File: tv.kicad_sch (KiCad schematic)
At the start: 38 parts, among them IC1 CXA1145, IC29 74HC4024, IC30 74HC10, U1 Conn_01x07, X1 4.433619MHz

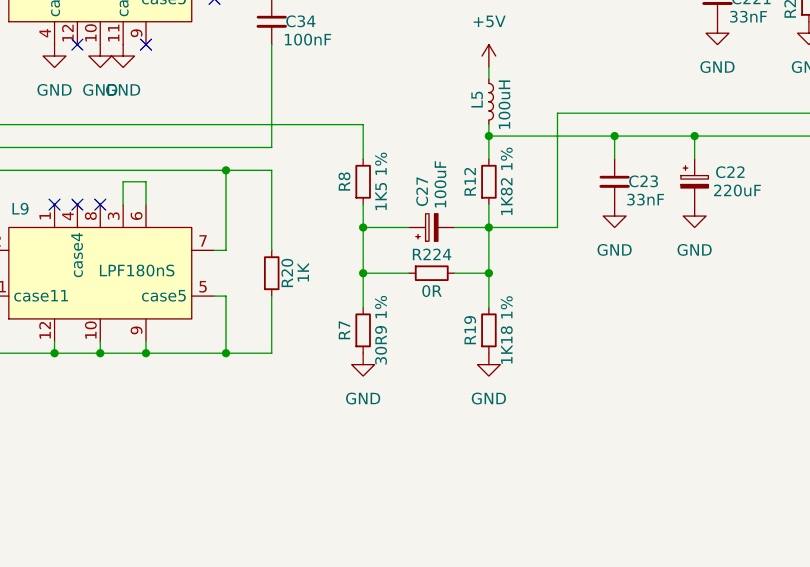
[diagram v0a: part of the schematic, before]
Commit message: video and keyboard routing
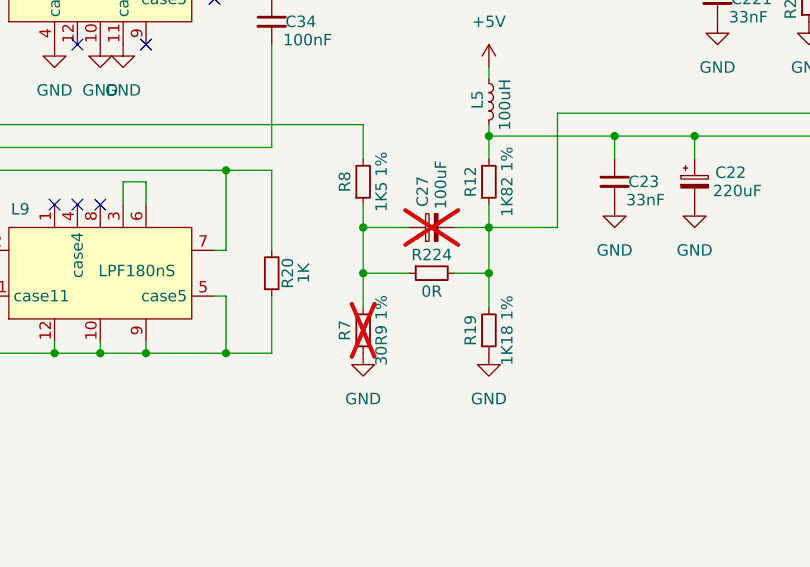
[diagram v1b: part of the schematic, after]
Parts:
- C25: footprint (none) -> Acorn:Trim_Capacitor
- C27: footprint Capacitor_THT:CP_Radial_D5.0mm_P2.50mm -> Capacitor_THT:CP_Radial_Tantal_D6.0mm_P5.00mm; now not fitted
- R7: now not fitted
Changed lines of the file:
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@@
 		(in_bom yes)
 		(on_board yes)
-		(dnp no)
+		(dnp yes)
 		(property "Reference" "R7"
 			(at 182.118 86.36 90)
@@
 		(in_bom yes)
 		(on_board yes)
-		(dnp no)
+		(dnp yes)
 		(property "Reference" "C27"
 			(at 190.754 72.644 0)
@@
 			)
 		)
-		(property "Footprint" "Capacitor_THT:CP_Radial_D5.0mm_P2.50mm"
+		(property "Footprint" "Capacitor_THT:CP_Radial_Tantal_D6.0mm_P5.00mm"
 			(at 191.77 74.93 0)
 			(effects
@@
 			)
 		)
-		(property "Footprint" ""
+		(property "Footprint" "Acorn:Trim_Capacitor"
 			(at 69.85 58.42 0)
 			(effects

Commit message: yet more traces
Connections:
- net TV_Sound: now also C220.2; no longer C220.1
- net at C221.1, R210.1, R211.2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: now also C220.1; no longer C220.2
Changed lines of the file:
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@@
 		(lib_id "Device:C_Polarized_Small")
 		(at 218.44 38.1 0)
+		(mirror x)
 		(unit 1)
 		(exclude_from_sim no)
@@
 		(dnp no)
 		(property "Reference" "C220"
-			(at 220.726 37.084 0)
+			(at 220.726 39.116 0)
 			(effects
 				(font
@@
 		)
 		(property "Value" "10uF"
-			(at 220.472 39.116 0)
+			(at 220.472 37.084 0)
 			(effects
 				(font

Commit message: keyboard routing
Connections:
- net +5V: now also IC30.14 (VCC)
- net GND: now also IC30.10, IC30.11, IC30.7 (GND), IC30.9
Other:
- moved on the sheet: IC30D

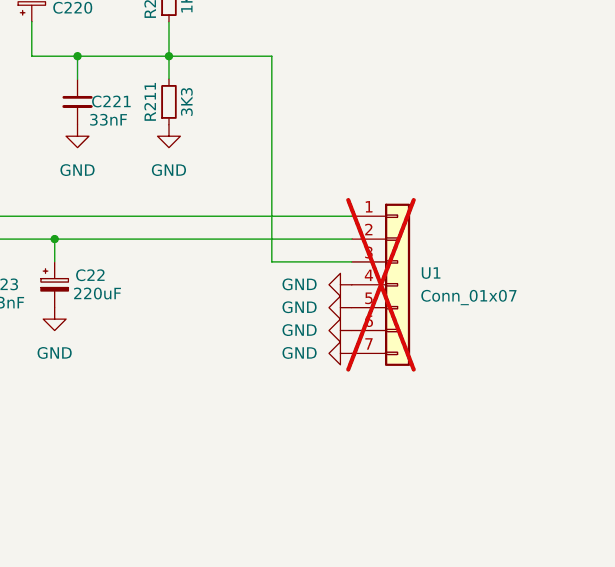
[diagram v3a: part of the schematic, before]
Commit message: progress power and keyboard
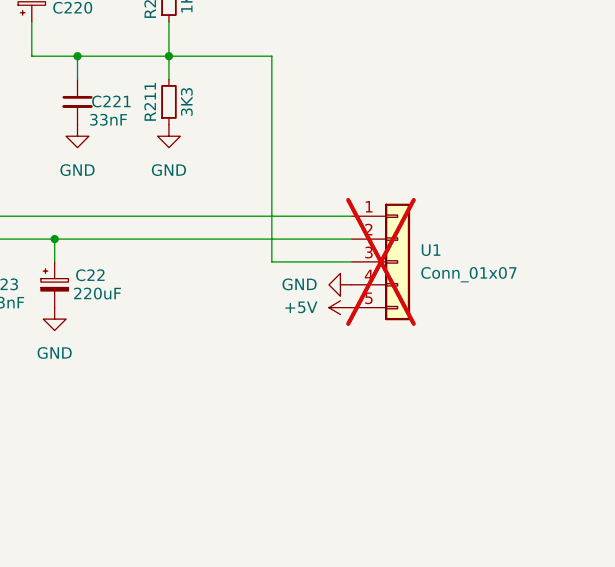
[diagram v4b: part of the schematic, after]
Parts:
- R12, R19, R7, R8: footprint Resistor_SMD:R_0805_2012Metric -> Resistor_SMD:R_1206_3216Metric
- U1: footprint Connector_PinSocket_2.54mm:PinSocket_1x07_P2.54mm_Vertical -> Connector_PinSocket_2.54mm:PinSocket_1x05_P2.54mm_Vertical; symbol Connector_Generic:Conn_01x07 -> Connector_Generic:Conn_01x05
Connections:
- net +5V: now also U1.5 (Pin_5)
- net GND: no longer U1.5 (Pin_5), U1.6 (Pin_6), U1.7 (Pin_7)

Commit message: analogue video
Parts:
- added R14: 1K, Resistor_SMD:R_0805_2012Metric, symbol Device:R_Small
- C33: footprint Capacitor_THT:CP_Radial_D5.0mm_P2.50mm -> Capacitor_THT:CP_Radial_Tantal_D4.5mm_P5.00mm
- IC1: footprint Package_SO:SOIC-24W_7.5x15.4mm_P1.27mm -> Package_SO:SOJ-24_7.62x15.875mm_P1.27mm
- L9: footprint (none) -> Acorn:LPF180nS
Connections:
- net GND: now also C25.1, R14.1; no longer C25.2
- net at C34.1, L7.7: now also R14.2
- net at IC1.6 (XIN), X1.1: now also C25.2; no longer C25.1
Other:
- moved on the sheet: C34
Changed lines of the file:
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@@
 	)
 	(junction
+		(at 171.45 44.45)
+		(diameter 0)
+		(color 0 0 0 0)
+	)
+	(junction
 		(at 120.65 88.9)
 		(diameter 0)
@@
 	(wire
 		(pts
+			(xy 171.45 44.45) (xy 180.34 44.45)
+		)
+		(stroke
+			(width 0)
+			(type default)
+		)
+	)
+	(wire
+		(pts
 			(xy 160.02 88.9) (xy 160.02 87.63)
 		)
@@
 	(wire
 		(pts
-			(xy 173.99 54.61) (xy 173.99 66.04)
+			(xy 171.45 54.61) (xy 171.45 66.04)
 		)
 		(stroke
@@
 	(wire
 		(pts
+			(xy 180.34 54.61) (xy 180.34 57.15)
+		)
+		(stroke
+			(width 0)
+			(type default)
+		)
+	)
+	(wire
+		(pts
 			(xy 194.31 74.93) (xy 198.12 74.93)
 		)
@@
 	(wire
 		(pts
-			(xy 173.99 44.45) (xy 167.64 44.45)
+			(xy 171.45 44.45) (xy 167.64 44.45)
 		)
 		(stroke
@@
 	(wire
 		(pts
-			(xy 173.99 49.53) (xy 173.99 44.45)
+			(xy 171.45 49.53) (xy 171.45 44.45)
 		)
 		(stroke
@@
 	(wire
 		(pts
-			(xy 134.62 66.04) (xy 173.99 66.04)
+			(xy 134.62 66.04) (xy 171.45 66.04)
 		)
 		(stroke
@@
 	(wire
 		(pts
+			(xy 180.34 44.45) (xy 180.34 49.53)
+		)
+		(stroke
+			(width 0)
+			(type default)
+		)
+	)
+	(wire
+		(pts
 			(xy 132.08 54.61) (xy 132.08 57.15)
 		)
@@
 			)
 		)
-		(property "Footprint" ""
+		(property "Footprint" "Acorn:LPF180nS"
 			(at 154.94 80.01 0)
 			(effects
@@
 	(symbol
 		(lib_id "power:GND")
+		(at 180.34 57.15 0)
+		(unit 1)
+		(exclude_from_sim no)
+		(in_bom yes)
+		(on_board yes)
+		(dnp no)
+		(fields_autoplaced yes)
+		(property "Reference" "#PWR0266"
+			(at 180.34 63.5 0)
+			(effects
+				(font
+					(size 1.27 1.27)
+				)
+				(hide yes)
+			)
+		)
+		(property "Value" "GND"
+			(at 180.34 62.23 0)
+			(effects
+				(font
+					(size 1.27 1.27)
+				)
+			)
+		)
+		(property "Footprint" ""
+			(at 180.34 57.15 0)
+			(effects
+				(font
+					(size 1.27 1.27)
+				)
+				(hide yes)
+			)
+		)
+		(property "Datasheet" ""
+			(at 180.34 57.15 0)
+			(effects
+				(font
+					(size 1.27 1.27)
+				)
+				(hide yes)
+			)
+		)
+		(property "Description" "Power symbol creates a global label with name \"GND\" , ground"
+			(at 180.34 57.15 0)
+			(effects
+				(font
+					(size 1.27 1.27)
+				)
+				(hide yes)
+			)
+		)
+		(pin "1"
+		)
+		(instances
+			(project "Acorn-A3010"
+				(path "/999882f3-94f8-4a89-9093-27a47d0cb289/2103e154-4875-4945-af52-f4b17646bf0d"
+					(reference "#PWR0266")
+					(unit 1)
+				)
+			)
+		)
+	)
+	(symbol
+		(lib_id "power:GND")
 		(at 120.65 99.06 0)
 		(unit 1)
@@
 			)
 		)
-		(property "Footprint" "Package_SO:SOIC-24W_7.5x15.4mm_P1.27mm"
+		(property "Footprint" "Package_SO:SOJ-24_7.62x15.875mm_P1.27mm"
 			(at 105.41 67.31 0)
 			(effects
@@
 	)
 	(symbol
+		(lib_id "Device:R_Small")
+		(at 180.34 52.07 0)
+		(mirror x)
+		(unit 1)
+		(exclude_from_sim no)
+		(in_bom yes)
+		(on_board yes)
+		(dnp no)
+		(property "Reference" "R14"
+			(at 182.118 52.07 90)
+			(effects
+				(font
+					(size 1.27 1.27)
+				)
+			)
+		)
+		(property "Value" "1K"
+			(at 183.896 52.07 90)
+			(effects
+				(font
+					(size 1.27 1.27)
+				)
+			)
+		)
+		(property "Footprint" "Resistor_SMD:R_0805_2012Metric"
+			(at 180.34 52.07 0)
+			(effects
+				(font
+					(size 1.27 1.27)
+				)
+				(hide yes)
+			)
+		)
+		(property "Datasheet" "~"
+			(at 180.34 52.07 0)
+			(effects
+				(font
+					(size 1.27 1.27)
+				)
+				(hide yes)
+			)
+		)
+		(property "Description" "Resistor, small symbol"
+			(at 180.34 52.07 0)
+			(effects
+				(font
+					(size 1.27 1.27)
+				)
+				(hide yes)
+			)
+		)
+		(pin "1"
+		)
+		(pin "2"
+		)
+		(instances
+			(project "Acorn-A3010"
+				(path "/999882f3-94f8-4a89-9093-27a47d0cb289/2103e154-4875-4945-af52-f4b17646bf0d"
+					(reference "R14")
+					(unit 1)
+				)
+			)
+		)
+	)
+	(symbol
 		(lib_id "Device:C_Polarized_Small")
 		(at 127 92.71 0)
@@
 			)
 		)
-		(property "Footprint" "Capacitor_THT:CP_Radial_D5.0mm_P2.50mm"
+		(property "Footprint" "Capacitor_THT:CP_Radial_Tantal_D4.5mm_P5.00mm"
 			(at 127 92.71 0)
 			(effects
@@
 	(symbol
 		(lib_id "Device:C_Small")
-		(at 173.99 52.07 0)
+		(at 171.45 52.07 0)
 		(mirror y)
 		(unit 1)
@@
 		(dnp no)
 		(property "Reference" "C34"
-			(at 175.514 52.07 0)
+			(at 172.974 52.07 0)
 			(effects
 				(font
@@
 		)
 		(property "Value" "100nF"
-			(at 175.26 54.102 0)
+			(at 172.72 54.102 0)
 			(effects
 				(font
@@
 		)
 		(property "Footprint" "Capacitor_SMD:C_0805_2012Metric"
-			(at 173.99 52.07 0)
+			(at 171.45 52.07 0)
 			(effects
 				(font
@@
 		)
 		(property "Datasheet" "~"
-			(at 173.99 52.07 0)
+			(at 171.45 52.07 0)
 			(effects
 				(font
@@
 		)
 		(property "Description" "Unpolarized capacitor, small symbol"
-			(at 173.99 52.07 0)
+			(at 171.45 52.07 0)
 			(effects
 				(font
@@
 		(lib_id "Device:C_Variable")
 		(at 69.85 58.42 0)
+		(mirror x)
 		(unit 1)
 		(exclude_from_sim no)
@@
 		(dnp no)
 		(property "Reference" "C25"
-			(at 72.644 57.15 0)
+			(at 72.644 59.69 0)
 			(effects
 				(font
@@
 		)
 		(property "Value" "5-55pF"
-			(at 72.644 59.69 0)
+			(at 72.644 57.15 0)
 			(effects
 				(font

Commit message: more analogue video work
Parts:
- added RF1: RF Modulator mounting, Acorn:Rf Modulator, symbol Mechanical:MountingHole
- L7: footprint (none) -> Acorn:BPF4_43M
- U1: value Conn_01x07 -> Analog Video breakout; footprint Connector_PinSocket_2.54mm:PinSocket_1x05_P2.54mm_Vertical -> Connector_PinSocket_2.54mm:PinSocket_1x07_P2.54mm_Vertical; symbol Connector_Generic:Conn_01x05 -> Connector_Generic_MountingPin:Conn_01x07_MountingPin
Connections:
- net +5V: no longer U1.5 (Pin_5)
- net CompB: now also U1.5 (Pin_5)
- net CompG: now also U1.6 (Pin_6)
- net CompR: now also U1.7 (Pin_7)
- net V_Filtered: now reaches C22.1, C23.1, L5.2, R12.2, U1.2 (Pin_2)
- net Composite: now reaches C27.2, R12.1, R19.2, R224.2, U1.1 (Pin_1)
- net Audio: now reaches C220.1, C221.1, R210.1, R211.2, U1.3 (Pin_3)
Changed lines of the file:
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@@
 	(wire
 		(pts
-			(xy 245.11 44.45) (xy 245.11 67.31)
+			(xy 243.84 44.45) (xy 243.84 67.31)
 		)
 		(stroke
@@
 	(wire
 		(pts
+			(xy 254 69.85) (xy 256.54 69.85)
+		)
+		(stroke
+			(width 0)
+			(type default)
+		)
+	)
+	(wire
+		(pts
 			(xy 189.23 80.01) (xy 184.15 80.01)
 		)
@@
 	(wire
 		(pts
-			(xy 205.74 62.23) (xy 254 62.23)
+			(xy 205.74 62.23) (xy 256.54 62.23)
 		)
 		(stroke
@@
 	(wire
 		(pts
-			(xy 245.11 44.45) (xy 233.68 44.45)
+			(xy 243.84 44.45) (xy 233.68 44.45)
 		)
 		(stroke
@@
 	(wire
 		(pts
+			(xy 243.84 67.31) (xy 256.54 67.31)
+		)
+		(stroke
+			(width 0)
+			(type default)
+		)
+	)
+	(wire
+		(pts
 			(xy 233.68 44.45) (xy 233.68 46.99)
 		)
@@
 	(wire
 		(pts
-			(xy 245.11 67.31) (xy 254 67.31)
-		)
-		(stroke
-			(width 0)
-			(type default)
-		)
-	)
-	(wire
-		(pts
 			(xy 168.91 77.47) (xy 167.64 77.47)
 		)
@@
 	(wire
 		(pts
-			(xy 220.98 64.77) (xy 254 64.77)
+			(xy 220.98 64.77) (xy 256.54 64.77)
 		)
 		(stroke
@@
 		)
 	)
+	(label "V_Filtered"
+		(at 232.41 64.77 0)
+		(fields_autoplaced yes)
+		(effects
+			(font
+				(size 1.27 1.27)
+			)
+			(justify left bottom)
+		)
+	)
+	(label "Composite"
+		(at 232.41 62.23 0)
+		(fields_autoplaced yes)
+		(effects
+			(font
+				(size 1.27 1.27)
+			)
+			(justify left bottom)
+		)
+	)
+	(label "Audio"
+		(at 245.11 67.31 0)
+		(fields_autoplaced yes)
+		(effects
+			(font
+				(size 1.27 1.27)
+			)
+			(justify left bottom)
+		)
+	)
 	(global_label "IV{slash}CS"
 		(shape input)
@@
 		)
 	)
+	(global_label "CompB"
+		(shape input)
+		(at 256.54 72.39 180)
+		(fields_autoplaced yes)
+		(effects
+			(font
+				(size 1.27 1.27)
+			)
+			(justify right)
+		)
+		(property "Intersheetrefs" "${INTERSHEET_REFS}"
+			(at 247.0235 72.39 0)
+			(effects
+				(font
+					(size 1.27 1.27)
+				)
+				(justify right)
+				(hide yes)
+			)
+		)
+	)
+	(global_label "CompG"
+		(shape input)
+		(at 256.54 74.93 180)
+		(fields_autoplaced yes)
+		(effects
+			(font
+				(size 1.27 1.27)
+			)
+			(justify right)
+		)
+		(property "Intersheetrefs" "${INTERSHEET_REFS}"
+			(at 247.0235 74.93 0)
+			(effects
+				(font
+					(size 1.27 1.27)
+				)
+				(justify right)
+				(hide yes)
+			)
+		)
+	)
 	(global_label "CLK2"
 		(shape input)
@@
 	(global_label "CompR"
 		(shape input)
+		(at 256.54 77.47 180)
+		(fields_autoplaced yes)
+		(effects
+			(font
+				(size 1.27 1.27)
+			)
+			(justify right)
+		)
+		(property "Intersheetrefs" "${INTERSHEET_REFS}"
+			(at 247.0235 77.47 0)
+			(effects
+				(font
+					(size 1.27 1.27)
+				)
+				(justify right)
+				(hide yes)
+			)
+		)
+	)
+	(global_label "CompR"
+		(shape input)
 		(at 93.98 55.88 180)
 		(fields_autoplaced yes)
@@
 			)
 		)
-		(property "Footprint" ""
+		(property "Footprint" "Acorn:BPF4_43M"
 			(at 154.94 46.99 0)
 			(effects
@@
 	)
 	(symbol
-		(lib_id "power:+5V")
-		(at 254 72.39 90)
-		(unit 1)
-		(exclude_from_sim no)
-		(in_bom yes)
-		(on_board yes)
-		(dnp no)
-		(fields_autoplaced yes)
-		(property "Reference" "#PWR0265"
-			(at 257.81 72.39 0)
-			(effects
-				(font
-					(size 1.27 1.27)
-				)
-				(hide yes)
-			)
-		)
-		(property "Value" "+5V"
-			(at 250.19 72.3899 90)
-			(effects
-				(font
-					(size 1.27 1.27)
-				)
-				(justify left)
-			)
-		)
-		(property "Footprint" ""
-			(at 254 72.39 0)
-			(effects
-				(font
-					(size 1.27 1.27)
-				)
-				(hide yes)
-			)
-		)
-		(property "Datasheet" ""
-			(at 254 72.39 0)
-			(effects
-				(font
-					(size 1.27 1.27)
-				)
-				(hide yes)
-			)
-		)
-		(property "Description" "Power symbol creates a global label with name \"+5V\""
-			(at 254 72.39 0)
-			(effects
-				(font
-					(size 1.27 1.27)
-				)
-				(hide yes)
-			)
-		)
-		(pin "1"
-		)
-		(instances
-			(project "Acorn-A3010"
-				(path "/999882f3-94f8-4a89-9093-27a47d0cb289/2103e154-4875-4945-af52-f4b17646bf0d"
-					(reference "#PWR0265")
-					(unit 1)
-				)
-			)
-		)
-	)
-	(symbol
 		(lib_id "Device:C_Small")
 		(at 132.08 52.07 0)
@@
 	)
 	(symbol
-		(lib_id "Connector_Generic:Conn_01x05")
-		(at 259.08 67.31 0)
+		(lib_id "Connector_Generic_MountingPin:Conn_01x07_MountingPin")
+		(at 261.62 69.85 0)
 		(unit 1)
 		(exclude_from_sim no)
@@
 		(fields_autoplaced yes)
 		(property "Reference" "U1"
-			(at 261.62 66.0399 0)
+			(at 264.16 68.9355 0)
 			(effects
 				(font
@@
 			)
 		)
-		(property "Value" "Conn_01x07"
-			(at 261.62 68.5799 0)
+		(property "Value" "Analog Video breakout"
+			(at 264.16 71.4755 0)
 			(effects
 				(font
@@
 			)
 		)
-		(property "Footprint" "Connector_PinSocket_2.54mm:PinSocket_1x05_P2.54mm_Vertical"
-			(at 259.08 67.31 0)
+		(property "Footprint" "Connector_PinSocket_2.54mm:PinSocket_1x07_P2.54mm_Vertical"
+			(at 261.62 69.85 0)
 			(effects
 				(font
@@
 		)
 		(property "Datasheet" "~"
-			(at 259.08 67.31 0)
+			(at 261.62 69.85 0)
 			(effects
 				(font
@@
 			)
 		)
-		(property "Description" "Generic connector, single row, 01x05, script generated (kicad-library-utils/schlib/autogen/connector/)"
-			(at 259.08 67.31 0)
+		(property "Description" "Generic connectable mounting pin connector, single row, 01x07, script generated (kicad-library-utils/schlib/autogen/connector/)"
+			(at 261.62 69.85 0)
 			(effects
 				(font
@@
 		(pin "1"
 		)
+		(pin "6"
+		)
+		(pin "7"
+		)
+		(pin "MP"
+		)
 		(instances
 			(project ""
@@
 					(unit 1)
 				)
+			)
+		)
+	)
+	(symbol
+		(lib_id "Mechanical:MountingHole")
+		(at 34.29 128.27 0)
+		(unit 1)
+		(exclude_from_sim yes)
+		(in_bom no)
+		(on_board yes)
+		(dnp no)
+		(fields_autoplaced yes)
+		(property "Reference" "RF1"
+			(at 36.83 126.9999 0)
+			(effects
+				(font
+					(size 1.27 1.27)
+				)
+				(justify left)
+			)
+		)
+		(property "Value" "RF Modulator mounting"
+			(at 36.83 129.5399 0)
+			(effects
+				(font
+					(size 1.27 1.27)
+				)
+				(justify left)
+			)
+		)
+		(property "Footprint" "Acorn:Rf Modulator"
+			(at 34.29 128.27 0)
+			(effects
+				(font
+					(size 1.27 1.27)
+				)
+				(hide yes)
+			)
+		)
+		(property "Datasheet" "~"
+			(at 34.29 128.27 0)
+			(effects
+				(font
+					(size 1.27 1.27)
+				)
+				(hide yes)
+			)
+		)
+		(property "Description" "Mounting Hole without connection"
+			(at 34.29 128.27 0)
+			(effects
+				(font
+					(size 1.27 1.27)
+				)
+				(hide yes)
+			)
+		)
+		(instances
+			(project ""
+				(path "/999882f3-94f8-4a89-9093-27a47d0cb289/2103e154-4875-4945-af52-f4b17646bf0d"
+					(reference "RF1")
+					(unit 1)
+				)

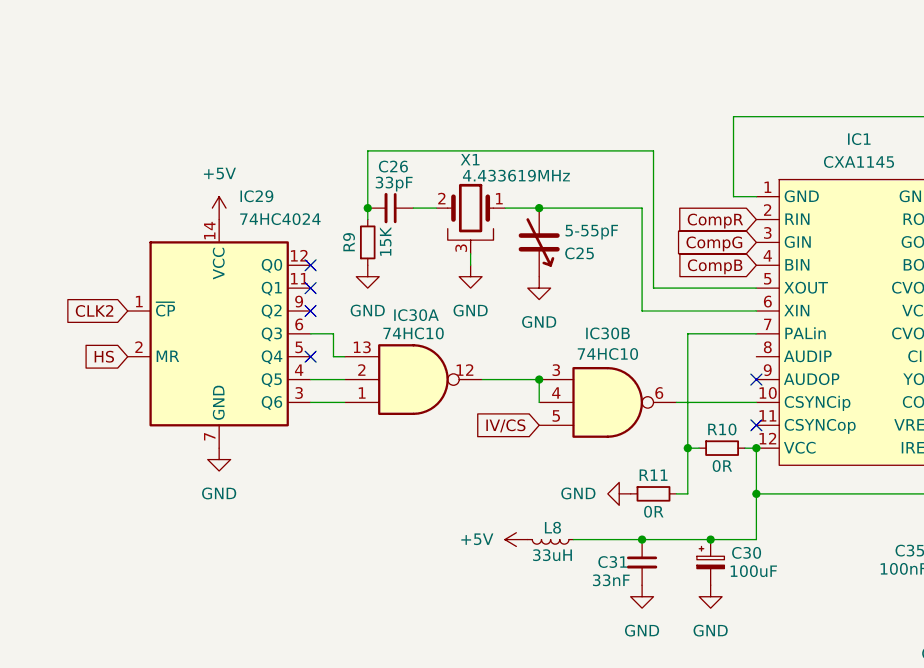
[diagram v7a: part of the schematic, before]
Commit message: adjust shielding perimeter trace and mounting holes
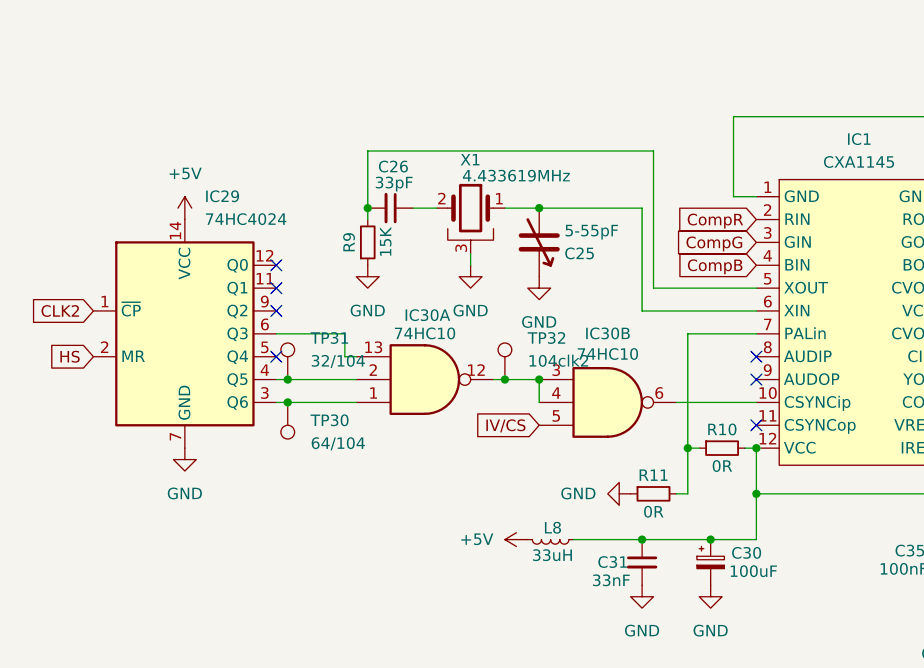
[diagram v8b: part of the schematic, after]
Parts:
- added TP30: 64/104, TestPoint:TestPoint_Pad_D1.0mm, symbol Connector:TestPoint
- added TP31: 32/104, TestPoint:TestPoint_Pad_D1.0mm, symbol Connector:TestPoint
- added TP32: 104clk2, TestPoint:TestPoint_Pad_D1.0mm, symbol Connector:TestPoint
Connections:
- net at IC30.12, IC30.3, IC30.4: now also TP32.1
- net at IC29.3 (Q6), IC30.1: now also TP30.1
- net at IC29.4 (Q5), IC30.2: now also TP31.1
- no-connect marks 18 -> 19
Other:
- moved on the sheet: IC29, IC30A
